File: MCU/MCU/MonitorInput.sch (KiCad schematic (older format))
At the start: 61 parts, among them J10 Conn_01x02, J5 Conn_01x04, J6 Conn_01x02, J7 Conn_01x02, J8 Conn_01x06, J9 Conn_01x06, U3 LMV324, U4 LMV324, U5 LMV358, U6 LMV324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

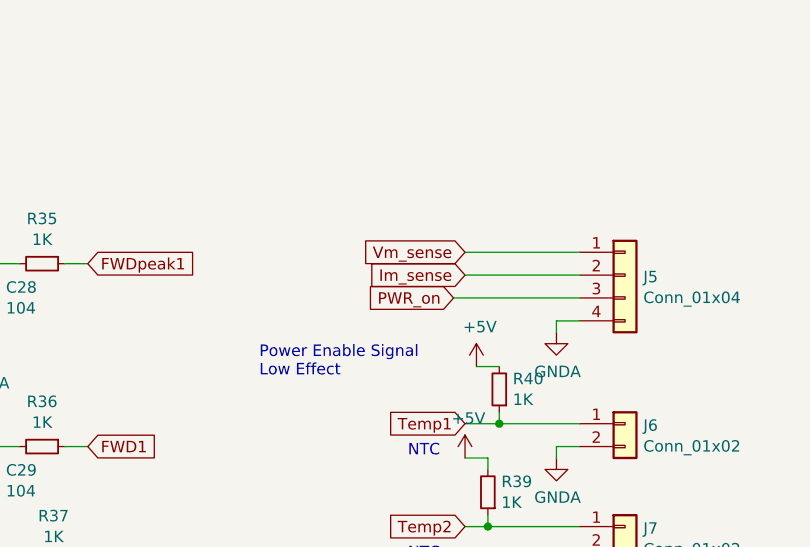
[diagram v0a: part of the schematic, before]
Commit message: MCU routed
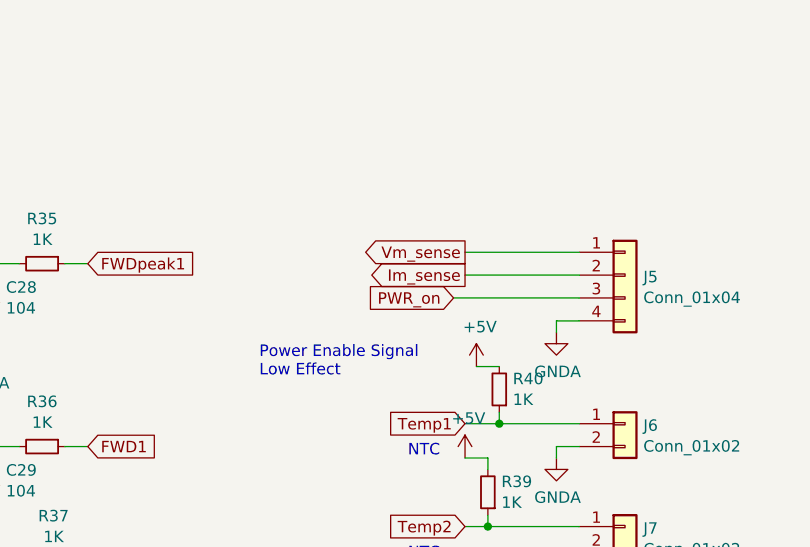
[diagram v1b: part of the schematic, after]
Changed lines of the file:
@@
 Text GLabel 8900 4800 0    50   Input ~ 0
 REV2
-Text GLabel 8900 1450 0    50   Input ~ 0
+Text GLabel 8900 1450 0    50   Output ~ 0
 Im_sense
-Text GLabel 8900 1350 0    50   Input ~ 0
+Text GLabel 8900 1350 0    50   Output ~ 0
 Vm_sense
 Text GLabel 8900 2100 0    50   Input ~ 0
@@
 	9000 2250 8900 2250
 $Comp
-L power:+5V #PWR061
-U 1 1 5E323ABA
-P 8900 2250
-F 0 "#PWR061" H 8900 2100 50  0001 C CNN
-F 1 "+5V" H 8915 2423 50  0000 C CNN
-F 2 "" H 8900 2250 50  0001 C CNN
-F 3 "" H 8900 2250 50  0001 C CNN
-	1    8900 2250
-	1    0    0    -1
-$EndComp
-$Comp
 L Device:R_Small R40
 U 1 1 5E325089
@@
 Wire Wire Line
 	9050 2100 9400 2100
-$Comp
-L power:+5V #PWR062
-U 1 1 5E331602
-P 8950 1850
-F 0 "#PWR062" H 8950 1700 50  0001 C CNN
-F 1 "+5V" H 8965 2023 50  0000 C CNN
-F 2 "" H 8950 1850 50  0001 C CNN
-F 3 "" H 8950 1850 50  0001 C CNN
-	1    8950 1850
-	1    0    0    -1
-$EndComp
 Wire Wire Line
 	8950 1850 9050 1850
@@
 Wire Wire Line
 	2400 7050 2600 7050
+$Comp
+L power:+5V #PWR062
+U 1 1 5E331602
+P 8950 1850
+F 0 "#PWR062" H 8950 1700 50  0001 C CNN
+F 1 "+5V" H 8965 2023 50  0000 C CNN
+F 2 "" H 8950 1850 50  0001 C CNN
+F 3 "" H 8950 1850 50  0001 C CNN
+	1    8950 1850
+	1    0    0    -1
+$EndComp
+$Comp
+L power:+5V #PWR061
+U 1 1 5E323ABA
+P 8900 2250
+F 0 "#PWR061" H 8900 2100 50  0001 C CNN
+F 1 "+5V" H 8915 2423 50  0000 C CNN
+F 2 "" H 8900 2250 50  0001 C CNN
+F 3 "" H 8900 2250 50  0001 C CNN
+	1    8900 2250
+	1    0    0    -1
+$EndComp
 $EndSCHEMATC
